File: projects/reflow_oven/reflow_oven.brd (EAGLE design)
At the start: 100 x 80 mm, 5 parts, among them IC1 MEGA32-A, IC3 FT232RL, X1 MINI-USB_SHIELD5P4-32005-400

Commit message: think the ftdi chip is done.  also did a good deal of the arduino setup.
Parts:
- added C2, C4, C9: 0.1uF, rcl:C0805
- added C3, C7, C8: 10uF, adafruit:175TMP-0810
- added C5, C6: 22pF, rcl:C0805
- added IC2: 7805DT, linear:TO252
- added LED1: Red, led:CHIPLED_0603
- added LED2: Green, led:CHIPLED_0603
- added POWERLED: Green, adafruit:CHIP-LED0805
- added R1, R2: 1k, resistor:R0805
- added R3: 10k, resistor:R0805
- added R4: 150, resistor:R0805
- added X2: 16.000MHz, adafruit:NX8045
- C1: value (none) -> 0.1uF; device rcl:C0805K -> rcl:C0805
- X1: value MINI-USB_SHIELD5P4-32005-400 -> USB; device con-cypressindustries:32005-400 -> con-cypressindustries:32005-201
- moved X1 36.1 mm to (6.35, 29.2), turned to 0 degrees
- moved C1 31.4 mm to (15.2, 30.5), turned to 270 degrees
- moved IC3 28.5 mm to (25.4, 21.6)
- moved IC1 23.6 mm to (44.5, 34.3), turned to 180 degrees
- moved S1 4.02 mm to (11.4, 6.35)
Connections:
- net RXD renamed 0
- net TXD renamed 1
- new net 10: IC1.42
- new net 11: IC1.43
- new net 12: IC1.44
- new net 13: IC1.1
- new net 8: IC1.40
- new net 9: IC1.41
- new net A1: IC1.23
- new net A2: IC1.22
- new net A3: IC1.21
- new net A4: IC1.20
- new net A5: IC1.19
- new net D+DP: IC3.15, X1.3
- new net D-DM: IC3.16, X1.2
- new net DTR: C4.2, IC3.2
- new net N$1: C5.2, IC1.7, X2.P$2
- new net N$10: IC1.15
- new net N$11: IC1.16
- new net N$17: IC1.24
- new net N$18: IC1.25
- new net N$19: IC1.26
- new net N$2: C6.2, IC1.8, X2.P$1
- new net N$4: LED1.A, R1.1
- new net N$5: POWERLED.C, R4.2
- new net N$6: IC1.11
- new net N$7: IC1.12
- new net N$8: IC1.13
- new net N$9: IC1.14
- new net POWER: IC3.4
- new net RXLED: IC3.22, LED2.C
- new net TXLED: IC3.23, LED1.C
- new net VIN: C7.+, IC2.1
- new net VOUT: C8.+, IC2.2, POWERLED.A
- net GND: now also C1.2, C2.2, C3.-, C5.1, C6.1, C7.-, C8.-, C9.1, IC2.3, IC3.26, R4.1, X1.5
- net N$3: now also LED2.A, R2.1; no longer C1.1, IC3.19
- net RESET: now also C4.1, R3.2; no longer C1.2
- net VCC: now also C2.1, C3.+, C9.2, IC1.29, R1.2, R2.2, R3.1, X1.1
- net VCCIO: now also C1.1, IC3.17; no longer IC3.4
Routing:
- net RESET: track 49.1 -> 0.00 mm
- net GND: track 42.1 -> 0.00 mm

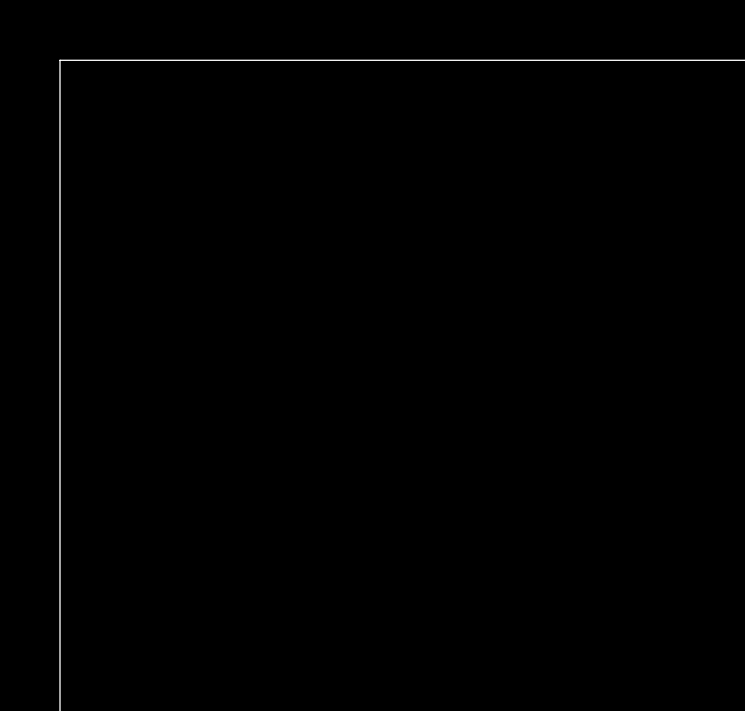
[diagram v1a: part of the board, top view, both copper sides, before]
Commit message: add DC Jack
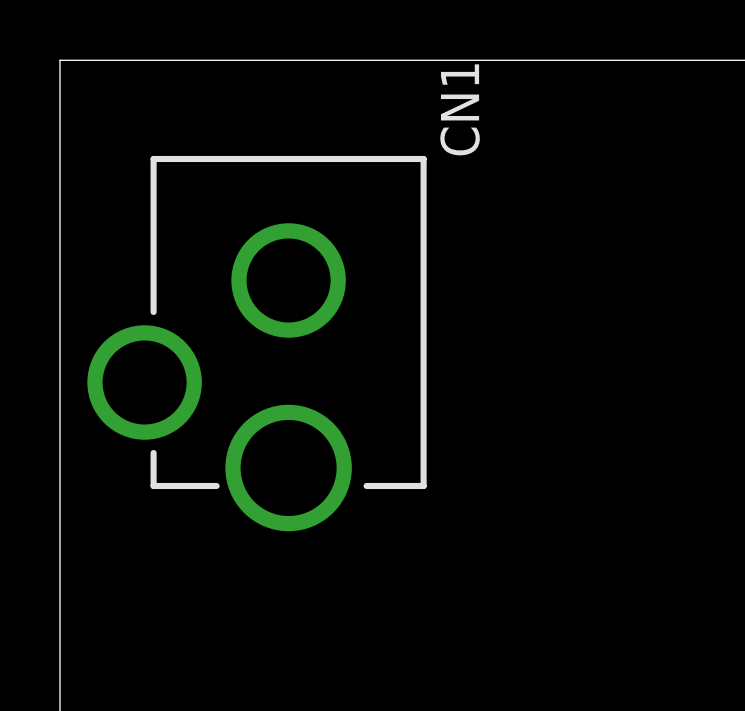
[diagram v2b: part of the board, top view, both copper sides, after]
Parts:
- added CN1: (no value), adafruit:DCJACK_2MM_PTH
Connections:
- net GND: now also CN1.GND, CN1.GNDBREAK
- net VIN: now also CN1.PWR
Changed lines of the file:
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@@
 <element name="R4" library="resistor" package="R0805" value="150" x="40.64" y="19.05" rot="R180"/>
 <element name="C9" library="rcl" package="C0805" value="0.1uF" x="55.88" y="26.67" rot="R270"/>
+<element name="CN1" library="adafruit" package="DCJACK_2MM_PTH" value="" x="7.62" y="80.01" rot="R180"/>
 </elements>
 <signals>
@@
 <contactref element="R4" pad="1"/>
 <contactref element="C9" pad="1"/>
+<contactref element="CN1" pad="GNDBREAK"/>
+<contactref element="CN1" pad="GND"/>
 <wire x1="63.5" y1="33.97" x2="63.5" y2="37.15" width="0" layer="19" extent="1-1"/>
 <wire x1="55.88" y1="27.62" x2="63.5" y2="33.97" width="0" layer="19" extent="1-1"/>
@@
 <wire x1="46.99" y1="2.85" x2="35.56" y2="2.85" width="0" layer="19" extent="1-1"/>
 <wire x1="2.85" y1="41.91" x2="9.35" y2="27.61" width="0" layer="19" extent="1-1"/>
+<wire x1="2.82" y1="69.26" x2="2.85" y2="41.91" width="0" layer="19" extent="1-1"/>
+<wire x1="7.62" y1="72.66" x2="2.82" y2="69.26" width="0" layer="19" extent="1-1"/>
 </signal>
 <signal name="VCC">
@@
 <contactref element="IC2" pad="1"/>
 <contactref element="C7" pad="+"/>
-<wire x1="27.68" y1="11.15" x2="35.56" y2="9.85" width="0" layer="19" extent="1-1"/>
+<contactref element="CN1" pad="PWR"/>
+<wire x1="27.68" y1="11.15" x2="7.62" y2="66.41" width="0" layer="19" extent="1-1"/>
+<wire x1="35.56" y1="9.85" x2="27.68" y2="11.15" width="0" layer="19" extent="1-1"/>
 </signal>
 <signal name="VOUT">

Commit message: button debounce start
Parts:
- added C10, C11: 1uF, resistor:C0805
- added C12: 100nF, resistor:C0805
- added D1, D2: (no value), adafruit:SMADIODE
- added IC4: 74HC14D, 74xx-eu:SO14
- added R5, R6: 82k, resistor:R0805
- added R7, R8: 18k, resistor:R0805
- added S2, S3: (no value), switch-omron:B3F-10XX
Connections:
- new net 2: IC4.10
- new net 3: IC4.12
- new net N$12: D1.A, R5.2, R8.1, S2.1, S2.2
- new net N$13: C11.1, D1.C, IC4.13, R8.2
- new net N$14: D2.A, R6.2, R7.1, S3.1, S3.2
- new net N$15: C10.1, D2.C, IC4.11, R7.2
- net GND: now also C10.2, C11.2, C12.2, IC4.7, S2.3, S2.4, S3.3, S3.4
- net VCC: now also C12.1, IC4.14, R5.1, R6.1
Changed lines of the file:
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@@
 <element name="C9" library="rcl" package="C0805" value="0.1uF" x="55.88" y="26.67" rot="R270"/>
 <element name="CN1" library="adafruit" package="DCJACK_2MM_PTH" value="" x="7.62" y="80.01" rot="R180"/>
+<element name="IC4" library="74xx-eu" package="SO14" value="74HC14D" x="67.31" y="15.24"/>
+<element name="R5" library="resistor" package="R0805" value="82k" x="76.2" y="30.48"/>
+<element name="R8" library="resistor" package="R0805" value="18k" x="92.71" y="29.21"/>
+<element name="D1" library="adafruit" package="SMADIODE" value="" x="77.47" y="48.26"/>
+<element name="C11" library="resistor" package="C0805" value="1uF" x="85.09" y="13.97"/>
+<element name="C12" library="resistor" package="C0805" value="100nF" x="81.28" y="71.12"/>
+<element name="S2" library="switch-omron" package="B3F-10XX" value="" x="74.93" y="5.08">
+<attribute name="OC_NEWARK" value="36M3542" x="74.93" y="5.08" size="1.778" layer="27" display="off"/>
+<attribute name="MPN" value="B3F-1000" x="74.93" y="5.08" size="1.778" layer="27" display="off"/>
+<attribute name="MF" value="" x="74.93" y="5.08" size="1.778" layer="27" display="off"/>
+<attribute name="OC_FARNELL" value="176432" x="74.93" y="5.08" size="1.778" layer="27" display="off"/>
+</element>
+<element name="R6" library="resistor" package="R0805" value="82k" x="92.71" y="39.37"/>
+<element name="R7" library="resistor" package="R0805" value="18k" x="88.9" y="54.61"/>
+<element name="D2" library="adafruit" package="SMADIODE" value="" x="74.93" y="58.42"/>
+<element name="C10" library="resistor" package="C0805" value="1uF" x="95.25" y="16.51"/>
+<element name="S3" library="switch-omron" package="B3F-10XX" value="" x="87.63" y="3.81">
+<attribute name="OC_NEWARK" value="36M3542" x="76.2" y="-1.27" size="1.778" layer="27" display="off"/>
+<attribute name="MPN" value="B3F-1000" x="76.2" y="-1.27" size="1.778" layer="27" display="off"/>
+<attribute name="MF" value="" x="76.2" y="-1.27" size="1.778" layer="27" display="off"/>
+<attribute name="OC_FARNELL" value="176432" x="76.2" y="-1.27" size="1.778" layer="27" display="off"/>
+</element>
 </elements>
 <signals>
@@
 <contactref element="CN1" pad="GNDBREAK"/>
 <contactref element="CN1" pad="GND"/>
+<contactref element="C11" pad="2"/>
+<contactref element="S2" pad="4"/>
+<contactref element="S2" pad="3"/>
+<contactref element="C10" pad="2"/>
+<contactref element="S3" pad="4"/>
+<contactref element="S3" pad="3"/>
+<contactref element="IC4" pad="7"/>
+<contactref element="C12" pad="2"/>
+<wire x1="63.5" y1="37.15" x2="82.13" y2="71.12" width="0" layer="19" extent="1-1"/>
 <wire x1="63.5" y1="33.97" x2="63.5" y2="37.15" width="0" layer="19" extent="1-1"/>
 <wire x1="55.88" y1="27.62" x2="63.5" y2="33.97" width="0" layer="19" extent="1-1"/>
@@
 <wire x1="46.99" y1="2.85" x2="35.56" y2="2.85" width="0" layer="19" extent="1-1"/>
 <wire x1="2.85" y1="41.91" x2="9.35" y2="27.61" width="0" layer="19" extent="1-1"/>
+<wire x1="71.12" y1="12.1666" x2="55.88" y2="27.62" width="0" layer="19" extent="1-1"/>
+<wire x1="71.6788" y1="2.8194" x2="71.12" y2="12.1666" width="0" layer="19" extent="1-1"/>
+<wire x1="78.1812" y1="2.8194" x2="71.6788" y2="2.8194" width="0" layer="19" extent="1-1"/>
+<wire x1="84.3788" y1="1.5494" x2="78.1812" y2="2.8194" width="0" layer="19" extent="1-1"/>
+<wire x1="90.8812" y1="1.5494" x2="84.3788" y2="1.5494" width="0" layer="19" extent="1-1"/>
+<wire x1="85.94" y1="13.97" x2="84.3788" y2="1.5494" width="0" layer="19" extent="1-1"/>
+<wire x1="96.1" y1="16.51" x2="85.94" y2="13.97" width="0" layer="19" extent="1-1"/>
 <wire x1="2.82" y1="69.26" x2="2.85" y2="41.91" width="0" layer="19" extent="1-1"/>
 <wire x1="7.62" y1="72.66" x2="2.82" y2="69.26" width="0" layer="19" extent="1-1"/>
@@
 <contactref element="IC1" pad="27"/>
 <contactref element="C9" pad="2"/>
+<contactref element="R5" pad="1"/>
+<contactref element="R6" pad="1"/>
+<contactref element="IC4" pad="14"/>
+<contactref element="C12" pad="1"/>
+<wire x1="91.86" y1="39.37" x2="80.43" y2="71.12" width="0" layer="19" extent="1-1"/>
+<wire x1="75.35" y1="30.48" x2="91.86" y2="39.37" width="0" layer="19" extent="1-1"/>
+<wire x1="63.5" y1="18.3134" x2="75.35" y2="30.48" width="0" layer="19" extent="1-1"/>
+<wire x1="55.88" y1="25.72" x2="63.5" y2="18.3134" width="0" layer="19" extent="1-1"/>
+<wire x1="50.25" y1="33.49" x2="55.88" y2="25.72" width="0" layer="19" extent="1-1"/>
 <wire x1="43.65" y1="28.49" x2="50.25" y2="33.49" width="0" layer="19" extent="1-1"/>
 <wire x1="38.65" y1="33.49" x2="43.65" y2="28.49" width="0" layer="19" extent="1-1"/>
 <wire x1="38.65" y1="35.09" x2="38.65" y2="33.49" width="0" layer="19" extent="1-1"/>
 <wire x1="44.45" y1="40.09" x2="38.65" y2="35.09" width="0" layer="19" extent="1-1"/>
-<wire x1="55.88" y1="25.72" x2="50.25" y2="33.49" width="0" layer="19" extent="1-1"/>
 <wire x1="21.775" y1="22.565" x2="38.65" y2="33.49" width="0" layer="19" extent="1-1"/>
 <wire x1="15.24" y1="23.18" x2="21.775" y2="22.565" width="0" layer="19" extent="1-1"/>
@@
 <contactref element="IC1" pad="26"/>
 </signal>
+<signal name="N$12">
+<contactref element="R5" pad="2"/>
+<contactref element="D1" pad="A"/>
+<contactref element="R8" pad="1"/>
+<contactref element="S2" pad="2"/>
+<contactref element="S2" pad="1"/>
+<wire x1="77.05" y1="30.48" x2="79.8195" y2="48.26" width="0" layer="19" extent="1-1"/>
+<wire x1="91.86" y1="29.21" x2="77.05" y2="30.48" width="0" layer="19" extent="1-1"/>
+<wire x1="78.1812" y1="7.3406" x2="77.05" y2="30.48" width="0" layer="19" extent="1-1"/>
+<wire x1="71.6788" y1="7.3406" x2="78.1812" y2="7.3406" width="0" layer="19" extent="1-1"/>
+</signal>
+<signal name="N$13">
+<contactref element="D1" pad="C"/>
+<contactref element="R8" pad="2"/>
+<contactref element="C11" pad="1"/>
+<contactref element="IC4" pad="13"/>
+<wire x1="93.56" y1="29.21" x2="75.1205" y2="48.26" width="0" layer="19" extent="1-1"/>
+<wire x1="84.24" y1="13.97" x2="93.56" y2="29.21" width="0" layer="19" extent="1-1"/>
+<wire x1="64.77" y1="18.3134" x2="84.24" y2="13.97" width="0" layer="19" extent="1-1"/>
+</signal>
+<signal name="N$14">
+<contactref element="R6" pad="2"/>
+<contactref element="D2" pad="A"/>
+<contactref element="R7" pad="1"/>
+<contactref element="S3" pad="2"/>
+<contactref element="S3" pad="1"/>
+<wire x1="77.2795" y1="58.42" x2="88.05" y2="54.61" width="0" layer="19" extent="1-1"/>
+<wire x1="93.56" y1="39.37" x2="88.05" y2="54.61" width="0" layer="19" extent="1-1"/>
+<wire x1="90.8812" y1="6.0706" x2="93.56" y2="39.37" width="0" layer="19" extent="1-1"/>
+<wire x1="84.3788" y1="6.0706" x2="90.8812" y2="6.0706" width="0" layer="19" extent="1-1"/>
+</signal>
+<signal name="N$15">
+<contactref element="D2" pad="C"/>
+<contactref element="R7" pad="2"/>
+<contactref element="C10" pad="1"/>
+<contactref element="IC4" pad="11"/>
+<wire x1="72.5805" y1="58.42" x2="89.75" y2="54.61" width="0" layer="19" extent="1-1"/>
+<wire x1="94.4" y1="16.51" x2="89.75" y2="54.61" width="0" layer="19" extent="1-1"/>
+<wire x1="67.31" y1="18.3134" x2="94.4" y2="16.51" width="0" layer="19" extent="1-1"/>
+</signal>
+<signal name="2">
+<contactref element="IC4" pad="10"/>
+</signal>
+<signal name="3">
+<contactref element="IC4" pad="12"/>
+</signal>
 </signals>

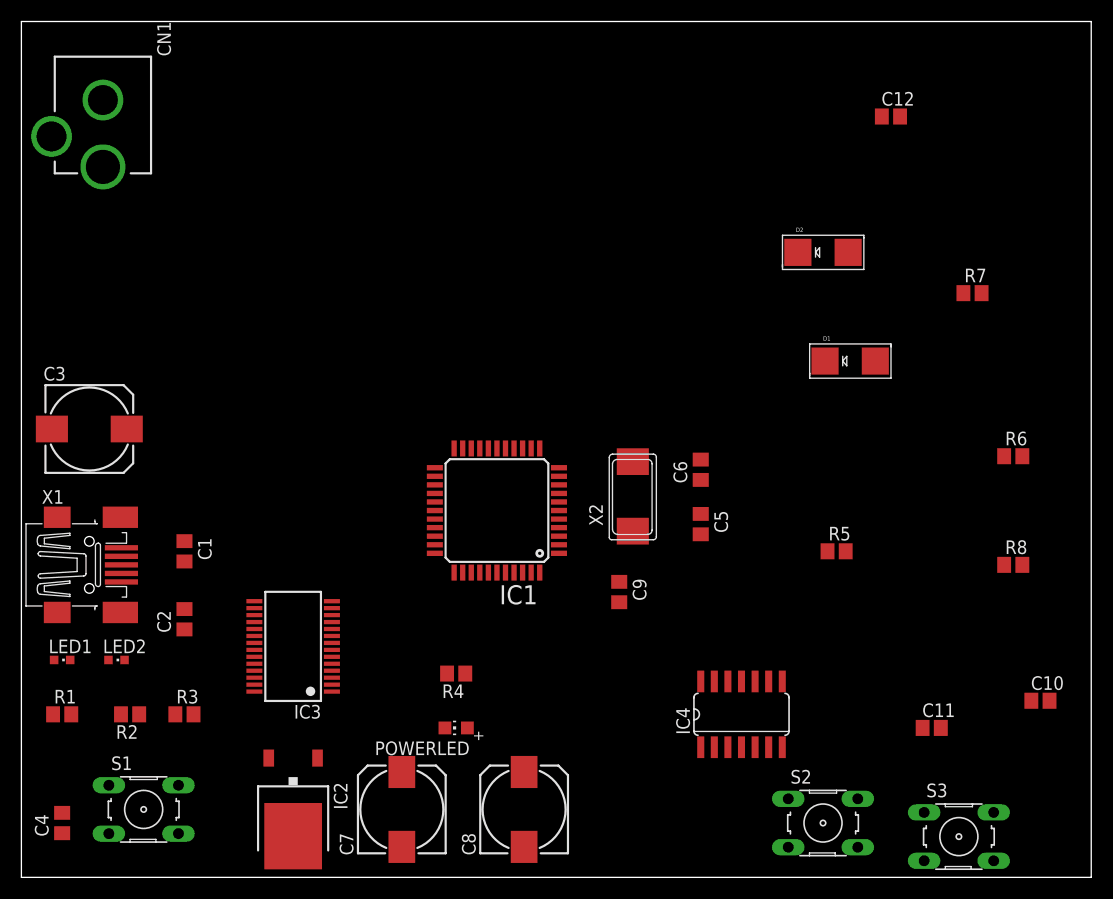
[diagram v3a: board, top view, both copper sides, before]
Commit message: better layout of board
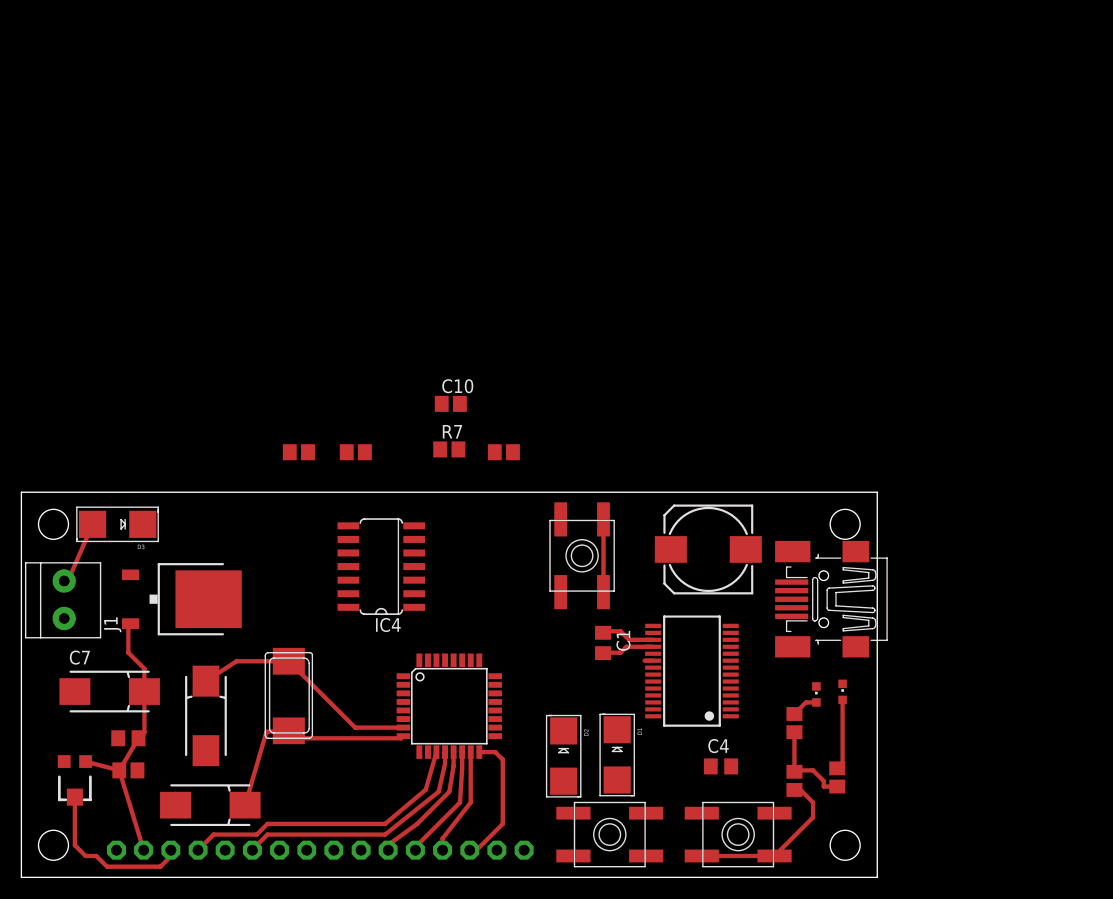
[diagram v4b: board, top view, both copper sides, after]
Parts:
- removed C8: 10uF, adafruit:175TMP-0810
- removed C9: 0.1uF, rcl:C0805
- removed CN1: (no value), adafruit:DCJACK_2MM_PTH
- removed POWERLED: Green, adafruit:CHIP-LED0805
- removed R3: 10k, resistor:R0805
- removed R4: 150, resistor:R0805
- removed S1: RESET, switch-omron:B3F-10XX
- removed S2, S3: (no value), switch-omron:B3F-10XX
- added D3: (no value), adafruit:SMADIODE
- added J1: 1X2-3.5MM, adafruit:1X2-3.5MM
- added JP1, JP2: (no value), adafruit:1X08-CLEANBIG
- added SW1: RST SW, adafruit:EVQ-Q2
- added SW2: D3 SW, adafruit:EVQ-Q2
- added SW3: D2 SW, adafruit:EVQ-Q2
- added U$1: 10k, adafruit:TC33X
- C5, C6: device rcl:C0805 -> rcl:085CS_1AR
- C7: value 10uF -> (none); device adafruit:175TMP-0810 -> rcl:085CS_1AR
- IC1: value MEGA32-A -> MEGA8-AI; device atmel:TQFP44 -> atmel:TQFP32-08
- X2: value 16.000MHz -> 16MHz
- moved C12 93.9 mm to (10.0, 10.0)
- moved LED1 73.0 mm to (76.8, 17.3), turned to 0 degrees
- moved R1 72.7 mm to (76.3, 9.34), turned to 270 degrees
- moved X1 68.7 mm to (75.0, 26.0), turned to 180 degrees
- moved LED2 65.5 mm to (74.3, 17.1), turned to 0 degrees
- moved C11 64.5 mm to (25.9, 39.7), turned to 180 degrees
- moved R8 62.3 mm to (31.3, 39.7), turned to 180 degrees
- moved R2 62.1 mm to (72.3, 14.4), turned to 270 degrees
- moved C4 61.8 mm to (65.4, 10.4), turned to 0 degrees
- moved C10 61.7 mm to (40.1, 44.3)
- moved C3 58.9 mm to (64.2, 30.6), turned to 180 degrees
- moved C6 55.5 mm to (17.7, 6.75), turned to 0 degrees
- moved D2 53.0 mm to (50.7, 11.3), turned to 270 degrees
- moved R7 51.0 mm to (40.0, 40.0)
- moved C5 49.6 mm to (17.2, 15.1), turned to 90 degrees
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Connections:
- removed net N$1: C5.2, IC1.7, X2.P$2
- removed net N$11: IC1.16
- removed net N$17: IC1.24
- removed net N$18: IC1.25
- removed net N$19: IC1.26
- removed net N$2: C6.2, IC1.8, X2.P$1
- removed net N$5: POWERLED.C, R4.2
- removed net N$6: IC1.11
- removed net N$7: IC1.12
- removed net N$8: IC1.13
- removed net VCC: C12.1, C2.1, C3.+, C9.2, IC1.17, IC1.27, IC1.29, IC1.38, IC1.5, IC3.20, IC4.14, R1.2, R2.2, R3.1, R5.1, R6.1, X1.1
- removed net VOUT: C8.+, IC2.2, POWERLED.A
- new net 4: IC1.2
- new net 5: IC1.9
- new net 5V: C12.1, C2.1, C3.+, C7.+, IC1.18, IC1.4, IC1.6, IC2.2, IC3.20, IC4.14, JP1.2, JP2.7, R1.2, R2.2, R5.1, R6.1, U$1.1, X1.1
- new net 6: IC1.10
- new net 7: IC1.11, JP1.4
- new net A0: IC1.23
- new net L3: JP1.3, U$1.2
- new net PWRIN: D3.A, J1.2
- new net XTAL1: C5.+, IC1.7, X2.P$2
- new net XTAL2: C6.+, IC1.8, X2.P$1
- net 0: now also IC1.30; no longer IC1.9
- net 1: now also IC1.31; no longer IC1.10
- net 10: now also IC1.14, JP2.4; no longer IC1.42
- net 11: now also IC1.15, JP2.5; no longer IC1.43
- net 12: now also IC1.16, JP2.6; no longer IC1.44
- net 13: now also IC1.17; no longer IC1.1
- net 2: now also IC1.32
- net 3: now also IC1.1
- net 8: now also IC1.12, JP1.6; no longer IC1.40
- net 9: now also IC1.13, JP2.3; no longer IC1.41
- net A1: now also IC1.24; no longer IC1.23
- net A2: now also IC1.25; no longer IC1.22
- net A3: now also IC1.26; no longer IC1.21
- net A4: now also IC1.27; no longer IC1.20
- net A5: now also IC1.28; no longer IC1.19
- net GND: now also C5.-, C6.-, IC1.21, IC1.3, IC1.5, J1.1, JP1.1, JP1.5, JP2.8, SW1.B, SW1.B', SW2.A, SW2.A', SW3.A, SW3.A', U$1.3; no longer C5.1, C6.1, C8.-, C9.1, CN1.GND, CN1.GNDBREAK, IC1.18, IC1.28, IC1.39, IC1.6, R4.1, S1.1, S1.2, S2.3, S2.4, S3.3, S3.4
- net N$10: now also IC1.22; no longer IC1.15
- net N$12: now also SW2.B, SW2.B'; no longer S2.1, S2.2
- net N$14: now also SW3.B, SW3.B'; no longer S3.1, S3.2
- net N$9: now also IC1.19; no longer IC1.14
- net RESET: now also IC1.29, SW1.A, SW1.A'; no longer IC1.4, R3.2, S1.3, S1.4
- net VIN: now also D3.C; no longer C7.+, CN1.PWR
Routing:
- net 5V: track 0.00 -> 35.7 mm
- net 7: track 0.00 -> 27.1 mm
- net 8: track 0.00 -> 23.3 mm
- net XTAL1: track 0.00 -> 21.6 mm
- net XTAL2: track 0.00 -> 20.3 mm
- net N$12: track 0.00 -> 15.5 mm
- net L3: track 0.00 -> 15.3 mm
- net 12: track 0.00 -> 12.6 mm
- net 9: track 0.00 -> 12.1 mm
- net 10: track 0.00 -> 10.9 mm
- net 11: track 0.00 -> 10.1 mm
- net RESET: track 0.00 -> 8.05 mm
- net N$4: track 0.00 -> 6.61 mm
- net PWRIN: track 0.00 -> 6.13 mm
- net VCCIO: track 0.00 -> 5.38 mm
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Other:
- board size 100 x 80 mm -> 80 x 36 mm
